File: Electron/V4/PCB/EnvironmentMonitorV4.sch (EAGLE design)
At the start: 28 parts, among them U3 ELECTRONDUALNAMED, U5 CCS811, U6 BME280, U7 ALS-PT19, U8 ALS-PT19

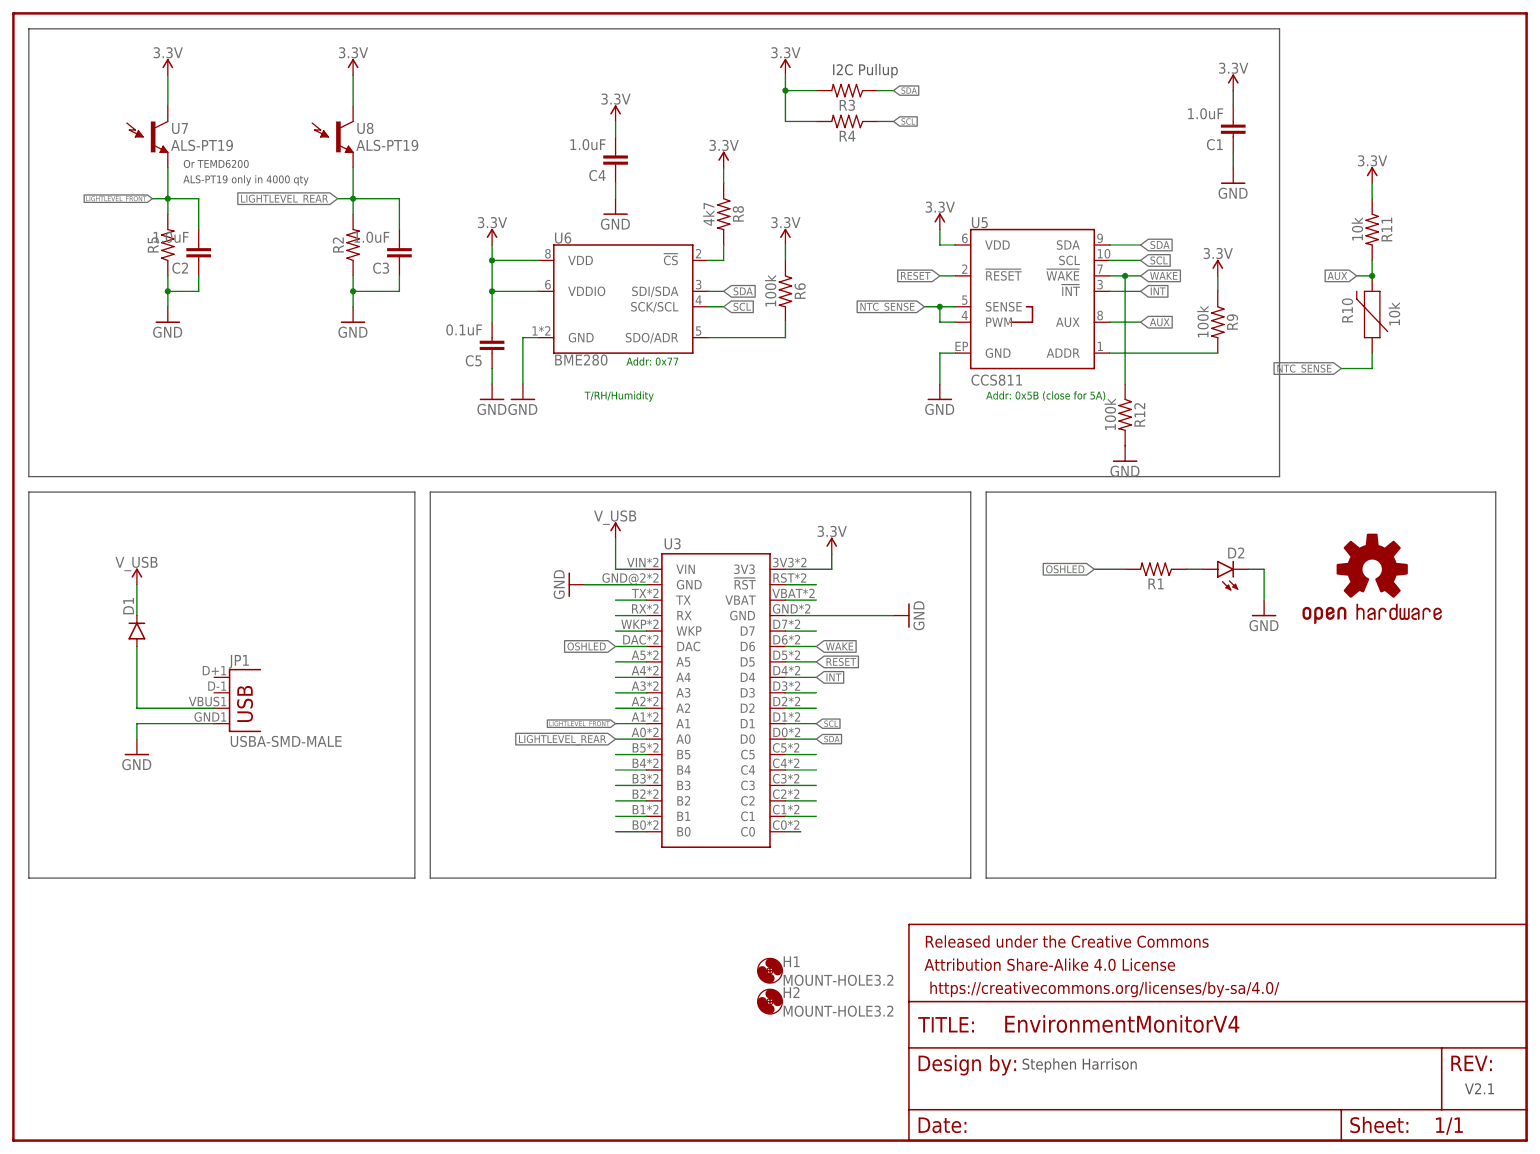
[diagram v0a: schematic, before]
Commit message: Update V4.0 PCB to use TEMT6000 rather than the diode which requires amplification, and removed rear sensor.
Ordered from DirtyPCBs.
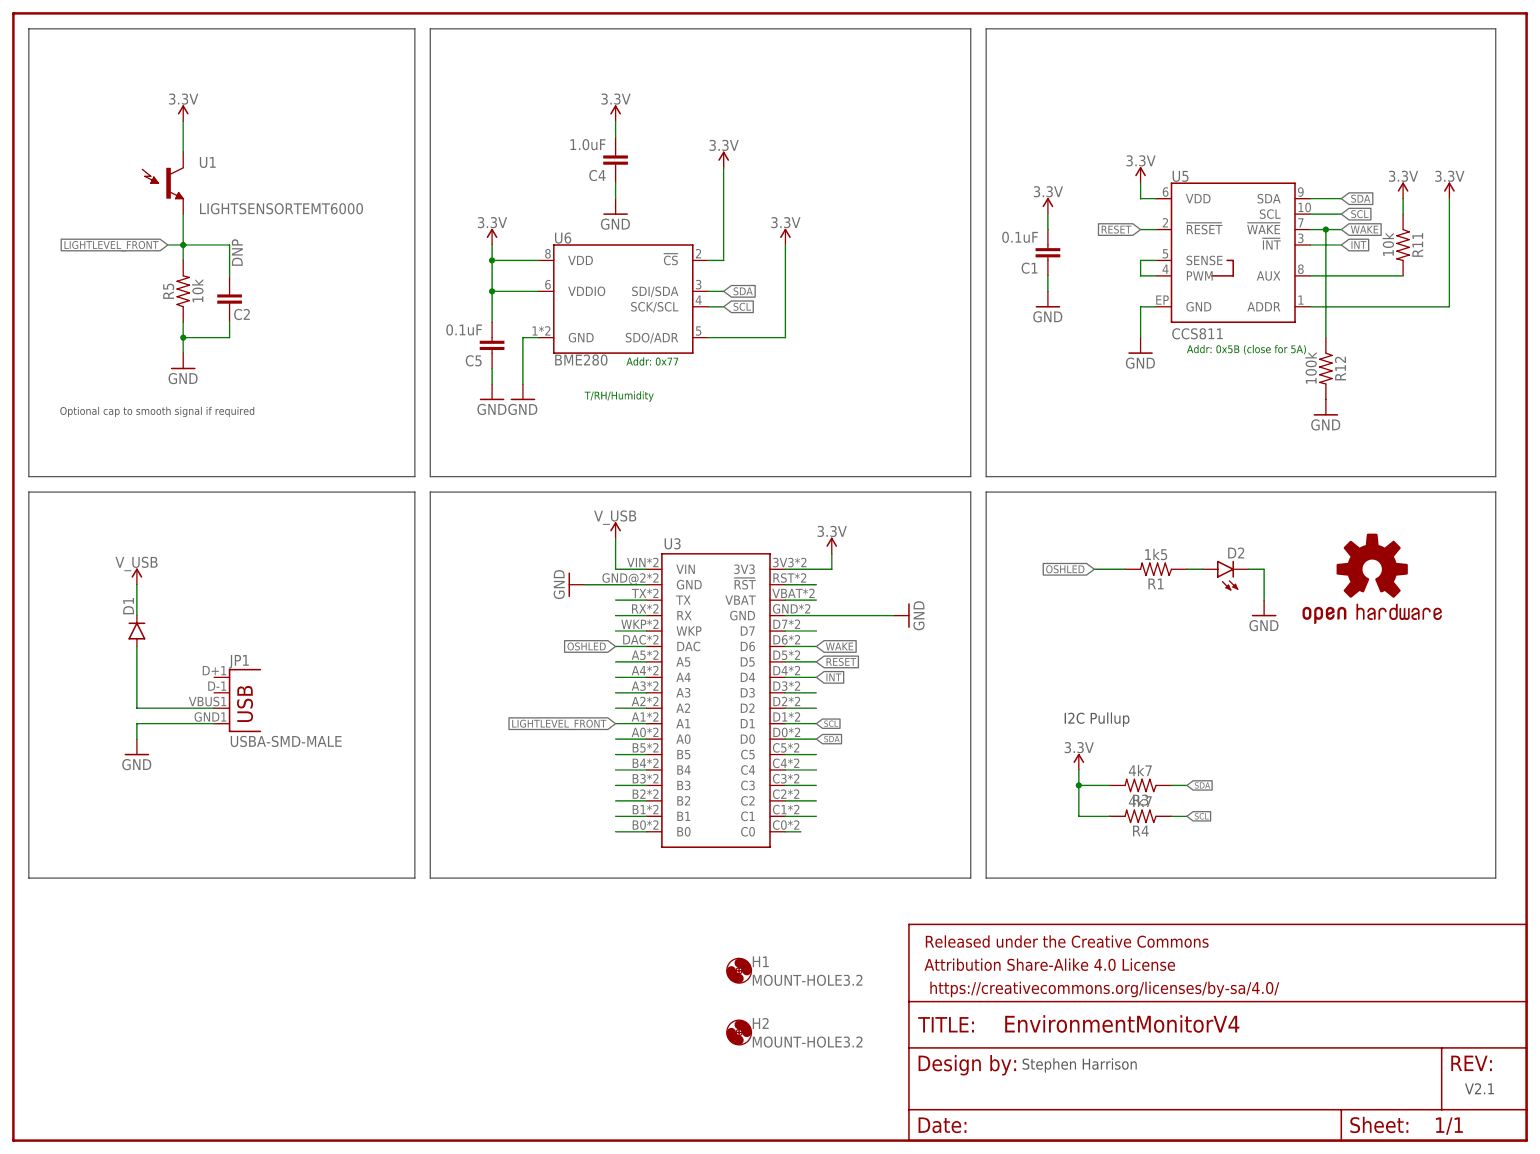
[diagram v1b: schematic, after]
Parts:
- removed C3: 1.0uF, SparkFun-Capacitors:1.0UF-25V-+80/-20(0805)"
- removed R10: 10k, CCS811_Breakout_Temp:NTC-THERMISTOR-0603
- removed R2: (no value), SparkFun-Resistors:RESISTOR0805
- removed R6, R9: 100k, SparkFun-Resistors:RESISTOR0805
- removed R8: 4k7, SparkFun-Resistors:RESISTOR0805
- removed U7, U8: ALS-PT19, SparkFun-Sensors:LIGHT_SENSORALS
- added U1: LIGHTSENSORTEMT6000, SparkFun-Sensors:LIGHTSENSORTEMT6000
- C1: value 1.0uF -> 0.1uF
- C2: value 1.0uF -> DNP
- R1: value (none) -> 1k5
- R3, R4: value (none) -> 4k7
- R5: value (none) -> 10k
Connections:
- removed net BME280_CS: R8.2, U6.!CS
- removed net N$3: R6.2, U6.SDO/ADR
- removed net N$9: R9.2, U5.ADDR
- net 3.3V: now also U1.C1, U5.ADDR, U6.!CS, U6.SDO/ADR; no longer R6.1, R8.1, R9.1, U7.C1, U8.C1
- net AUX: no longer R10.2
- net GND: no longer C3.1, R2.1
- net LIGHTLEVEL_FRONT: now also U1.E1; no longer U7.E1
- net LIGHTLEVEL_REAR: no longer C3.2, R2.2, U8.E1
- net NTC_SENSE: no longer R10.1
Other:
- note added: "Optional cap to smooth signal if required"
- note removed: "ALS-PT19 only in 4000 qty"
- note removed: "Or TEMD6200"
- moved on the sheet: C1, C2, H1, H2, R11, R12, R3, R4, R5, U5
